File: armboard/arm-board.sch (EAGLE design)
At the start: 50 parts, among them X1 53261-06

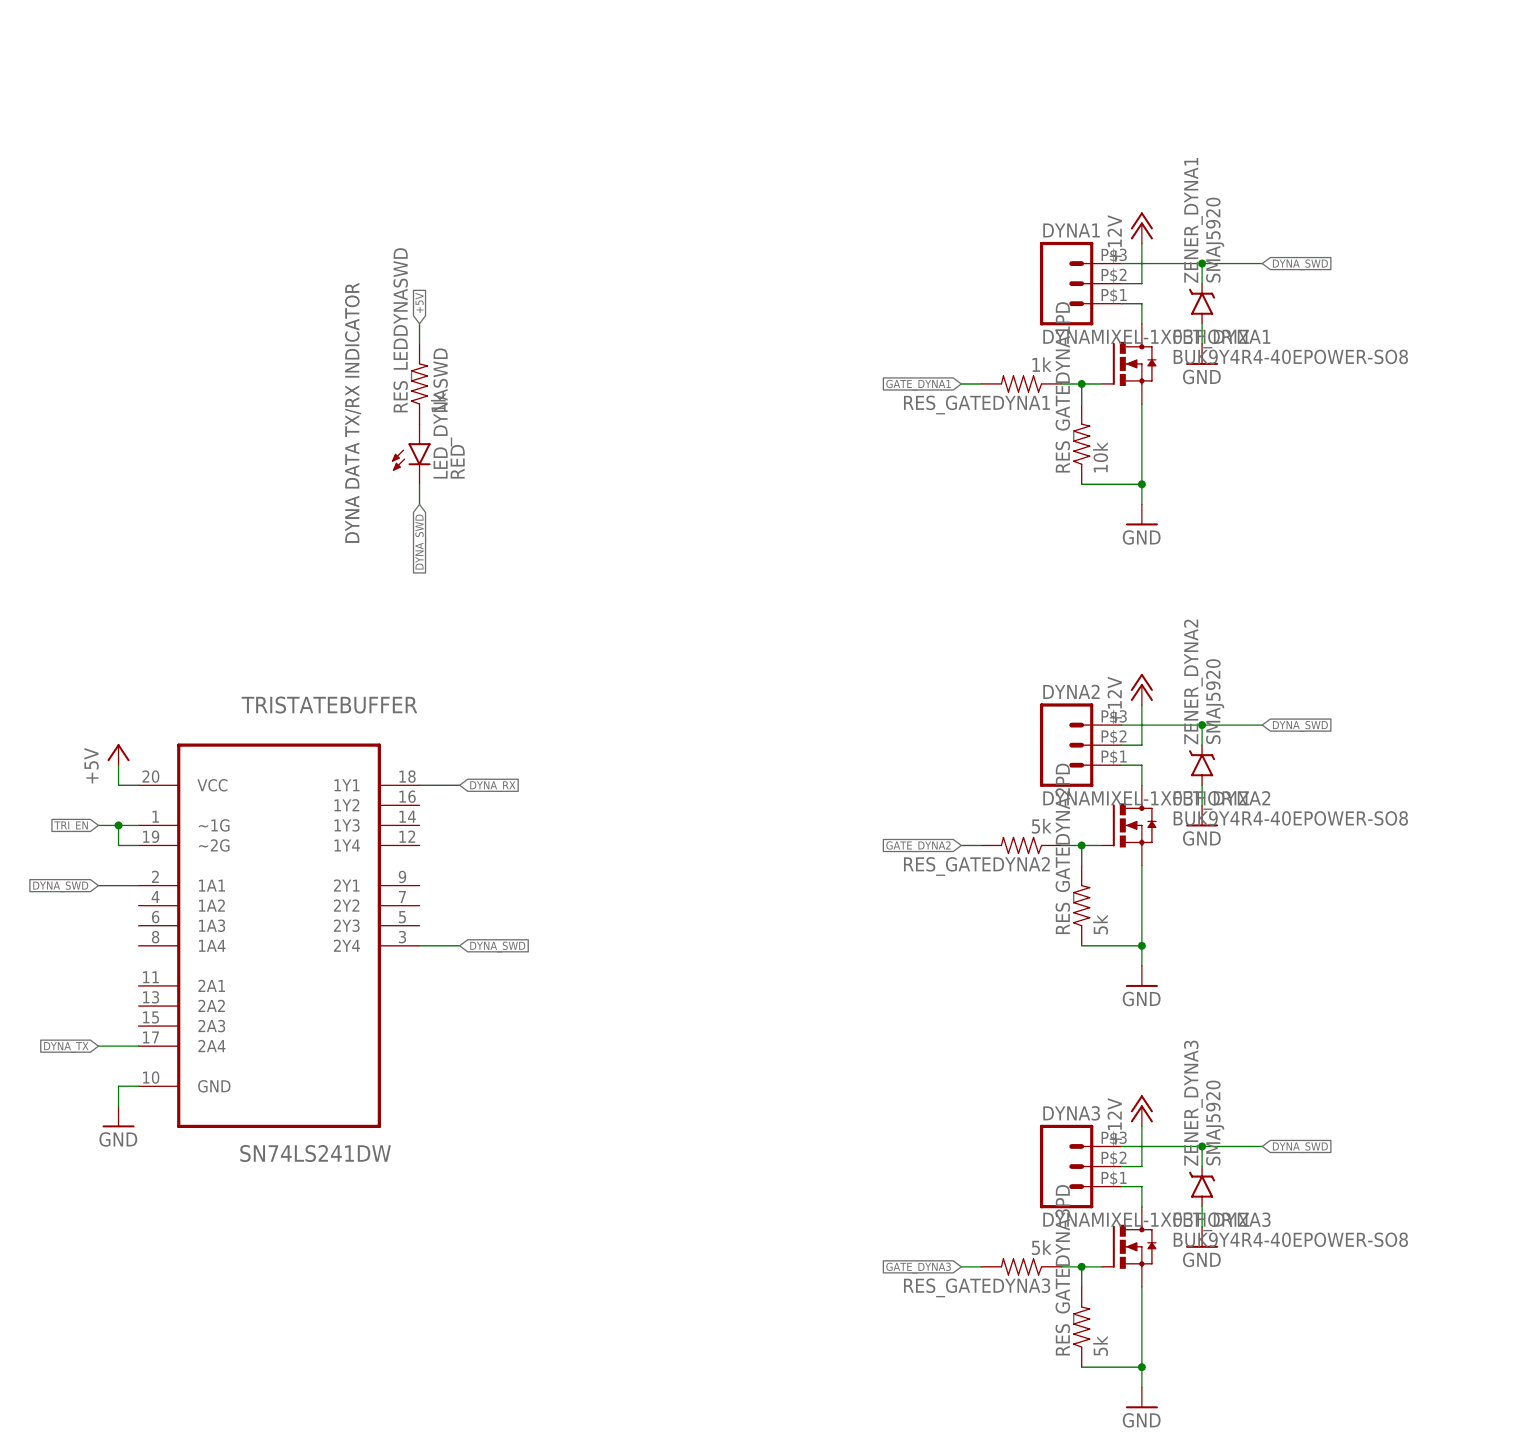
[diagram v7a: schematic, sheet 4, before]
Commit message: added high side fet drivers, rearranged
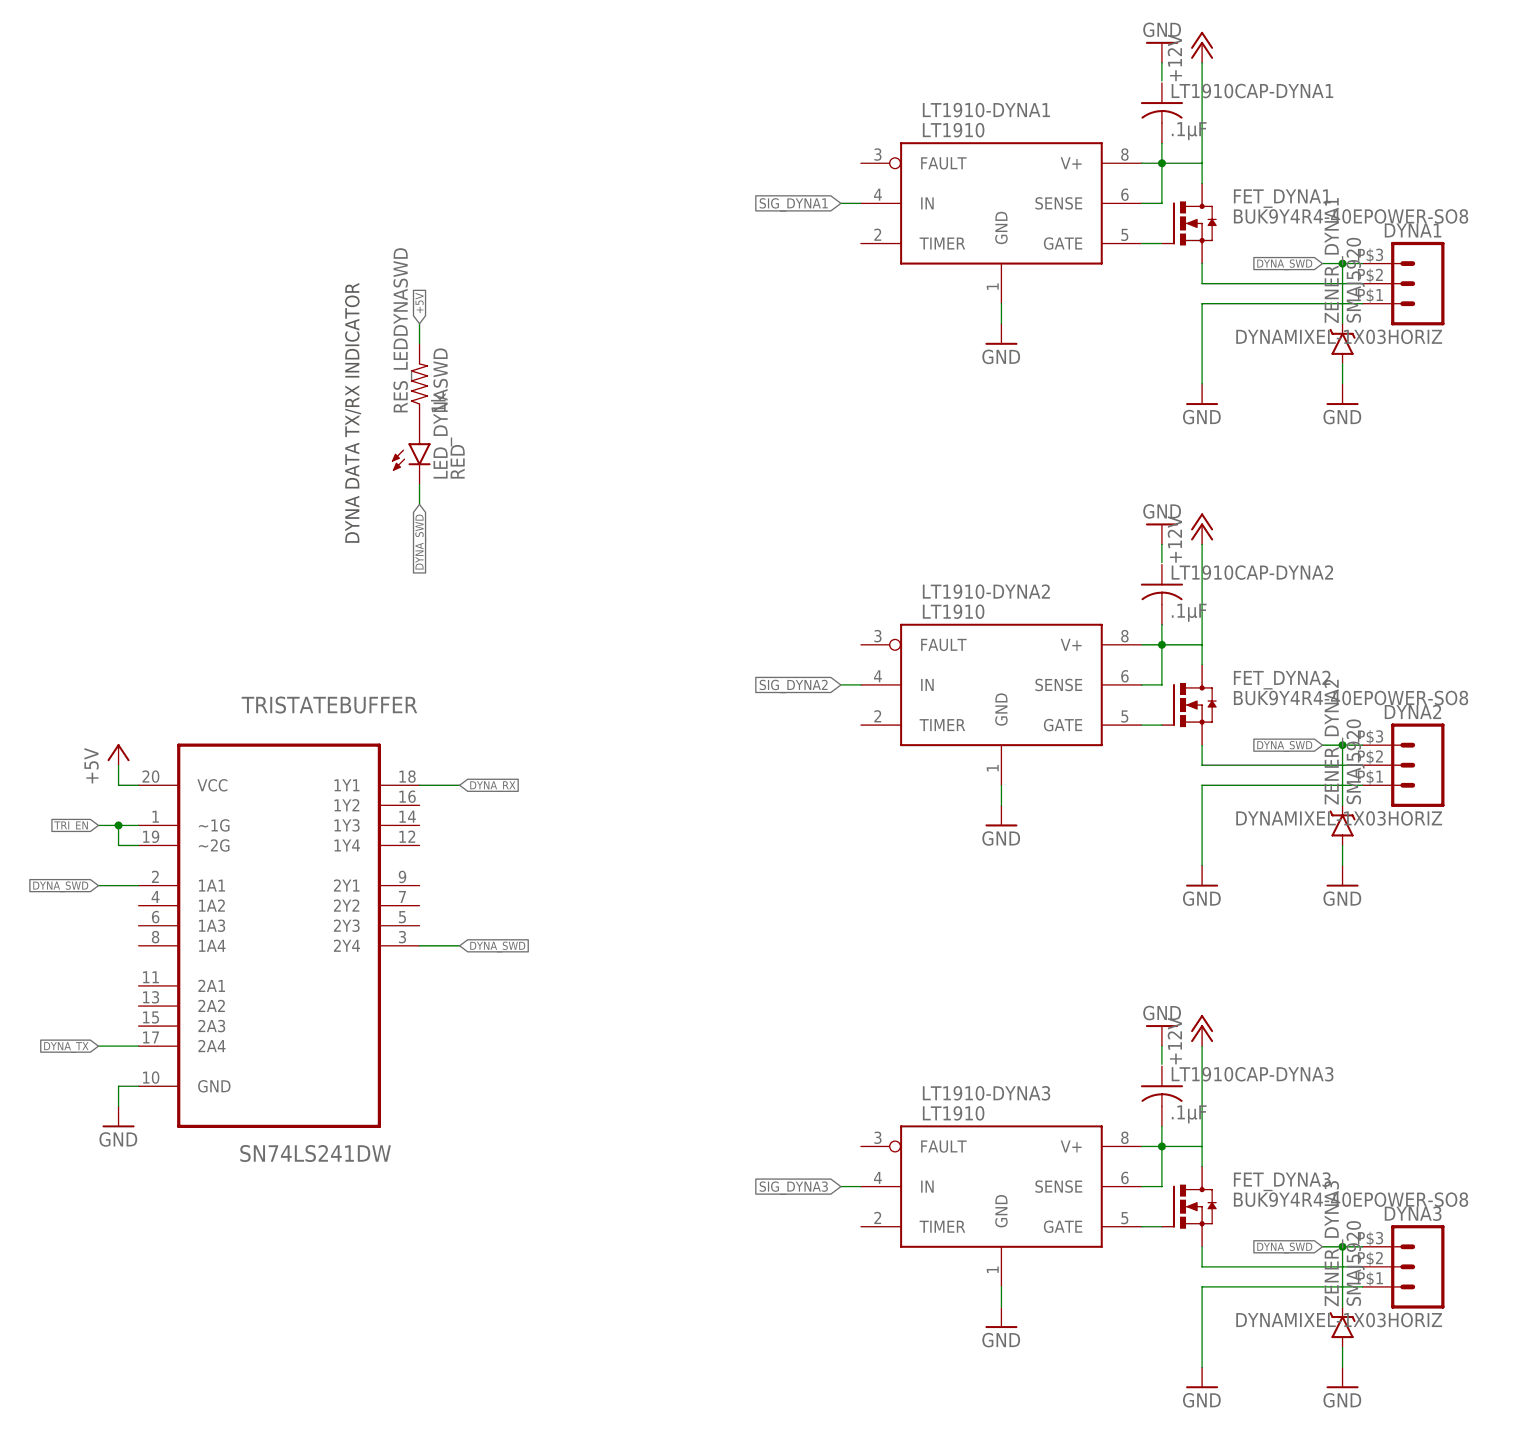
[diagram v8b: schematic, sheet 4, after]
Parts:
- removed C10, C11, C8, C9: 0.33uF, SparkFun-Capacitors:CAP1206
- removed C7: .047uF, SparkFun-Capacitors:CAP1206
- removed CON_PWR_MAIN_J2, CON_PWR_SOL_EE: MLX-2X3-PIN, MRDT-2015-General:MLX-2X3-PIN
- removed MAX232: MAX3232, MRDT-LIB2014:MAX3232
- removed RES_GATEDYNA1: 1k, SparkFun-Resistors:RESISTOR1206
- removed RES_GATEDYNA1PD: 10k, SparkFun-Resistors:RESISTOR1206
- removed RES_GATEDYNA2, RES_GATEDYNA2PD, RES_GATEDYNA3, RES_GATEDYNA3PD, RES_GATEPWREE, RES_GATEPWREEPD, RES_GATEPWRSOL, RES_GATEPWRSOLPD: 5k, SparkFun-Resistors:RESISTOR1206
- added EE-12V, J2_12V, SOL-12V: ANDERSON_POWERPOLEPP45_PCB_HORIZ_RIGHT_2HIGH, MRDT-Connectors:ANDERSON_POWERPOLEPP45_PCB_HORIZ_RIGHT_2HIGH
- added EE-GND, J2_GND, SOL-GND: ANDERSON_POWERPOLEPP45_PCB_HORIZ_RIGHT, MRDT-Connectors:ANDERSON_POWERPOLEPP45_PCB_HORIZ_RIGHT
- added LT1910-DYNA1, LT1910-DYNA2, LT1910-DYNA3, LT1910-EE, LT1910-SOL: LT1910, Jake:LT1910
- added LT1910CAP-DYNA1, LT1910CAP-DYNA2, LT1910CAP-DYNA3, LT1910CAP-EE, LT1910CAP-SOL: .1µF, resistor:C-USC1206
- added MAX232_1: MAX3232SO16, MRDT-Digital-ICs:MAX3232SO16
- added MAX232_C1_1: .047uF, SparkFun-Capacitors:CAP1206
- added MAX232_C2_1, MAX232_VNCAP_1, MAX232_VPCAP_1: 0.33uF, SparkFun-Capacitors:CAP1206
- added MAX232_DECAP_1: 0.1uF, SparkFun-Capacitors:CAP1206
- added PWR_MAIN: APP_3POS_CONFIG5V_12V_VERT, MRDT-Connectors:APP_3POS_CONFIG5V_12V_VERT
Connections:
- removed net DYNA1_GND: DYNA1.1, FET_DYNA1.D
- removed net DYNA1_GND1: DYNA2.1, FET_DYNA2.D
- removed net DYNA1_GND2: DYNA3.1, FET_DYNA3.D
- removed net EE_GND1: CON_PWR_SOL_EE.GND_2, FET_PWREE.D
- removed net GATE_DYNA1: RES_GATEDYNA1.2, U$1.PE2
- removed net GATE_DYNA2: RES_GATEDYNA2.2, U$1.PE3
- removed net GATE_DYNA3: RES_GATEDYNA3.2, U$1.PD7
- removed net GATE_PWR_EE: RES_GATEPWREE.2, U$1.PH0
- removed net GATE_PWR_SOL: RES_GATEPWRSOL.2, U$1.PH1
- removed net N$10: RES_GATEDYNA2.1, RES_GATEDYNA2PD.2
- removed net N$11: FET_PWREE.G, RES_GATEPWREE.1, RES_GATEPWREEPD.2
- removed net N$12: FET_DYNA3.G, RES_GATEDYNA3.1, RES_GATEDYNA3PD.2
- removed net N$15: C7.2, MAX232.C1-
- removed net N$16: C7.1, MAX232.C1+
- removed net N$17: C8.1, MAX232.C2+
- removed net N$18: C8.2, MAX232.C2-
- removed net N$19: C10.1, MAX232.V-
- removed net N$20: C9.1, MAX232.V+
- removed net N$5: CON_PWR_SOL_EE.12V_2
- removed net N$6: FET_DYNA1.G, RES_GATEDYNA1.1, RES_GATEDYNA1PD.2
- removed net N$7: FET_PWRSOL.G, RES_GATEPWRSOL.1, RES_GATEPWRSOLPD.2
- removed net R_OUT1: MAX232.R_OUT1, X1-2.S
- removed net SOL_GND1: CON_PWR_SOL_EE.GND_1, FET_PWRSOL.D
- removed net T_OUT1: MAX232.T_OUT1, X1-1.S
- removed net VCC1: C11.1, MAX232.VCC
- new net GATE-DYNA1: LT1910-DYNA1.GATE
- new net GATE-DYNA2: LT1910-DYNA2.GATE
- new net GATE-DYNA3: LT1910-DYNA3.GATE
- new net GATE-EE: LT1910-EE.GATE
- new net GATE-SOL: LT1910-SOL.GATE
- new net N$1_1: MAX232_1.C1+, MAX232_C1_1.1
- new net N$2_1: MAX232_1.V+, MAX232_VPCAP_1.1
- new net N$3_1: MAX232_1.C1-, MAX232_C1_1.2
- new net N$4_1: MAX232_1.C2+, MAX232_C2_1.1
- new net N$5_1: MAX232_1.C2-, MAX232_C2_1.2
- new net N$6_1: MAX232_1.V-, MAX232_VNCAP_1.1
- new net R1IN: MAX232_1.R1IN, X1-2.S
- new net SIG_DYNA1: LT1910-DYNA1.IN, U$1.PE2
- new net SIG_DYNA2: LT1910-DYNA2.IN, U$1.PE3
- new net SIG_DYNA3: LT1910-DYNA3.IN, U$1.PD7
- new net SIG_EE: LT1910-EE.IN, U$1.PH0
- new net SIG_SOL: LT1910-SOL.IN, U$1.PH1
- new net SOURCE-DYNA1: DYNA1.2, FET_DYNA1.S
- new net SOURCE-DYNA2: DYNA2.2, FET_DYNA2.S
- new net SOURCE-DYNA3: DYNA3.2, FET_DYNA3.S
- new net SOURCE-EE: EE-12V.P$1, FET_PWREE.S
- new net SOURCE-SOL: FET_PWRSOL.S, SOL-12V.P$1
- new net T1OUT: MAX232_1.T1OUT, X1-1.S
- net +12V: now also FET_DYNA1.D, FET_DYNA2.D, FET_DYNA3.D, FET_PWREE.D, FET_PWRSOL.D, J2_12V.P$1, LT1910-DYNA1.SENSE, LT1910-DYNA1.V+, LT1910-DYNA2.SENSE, LT1910-DYNA2.V+, LT1910-DYNA3.SENSE, LT1910-DYNA3.V+, LT1910-EE.SENSE, LT1910-EE.V+, LT1910-SOL.SENSE, LT1910-SOL.V+, LT1910CAP-DYNA1.2, LT1910CAP-DYNA2.2, LT1910CAP-DYNA3.2, LT1910CAP-EE.2, LT1910CAP-SOL.2, PWR_MAIN12V.P$1, RES_LEDPWR.2; no longer CON_PWR_MAIN_J2.12V_1, CON_PWR_MAIN_J2.12V_2, CON_PWR_SOL_EE.12V_1, DYNA1.2, DYNA2.2, DYNA3.2
- net +5V: now also MAX232_1.VCC, MAX232_DECAP_1.2, PWR_MAIN5V.P$1; no longer CON_PWR_MAIN_J2.5V_1, RES_LEDPWR.2
- net DYNA_RX: now also U$1.PC4; no longer U$1.PC6
- net DYNA_TX: now also U$1.PC5; no longer U$1.PC7
- net GND: now also DYNA1.1, DYNA2.1, DYNA3.1, EE-GND.P$1, J2_GND.P$1, LT1910-DYNA1.GND, LT1910-DYNA2.GND, LT1910-DYNA3.GND, LT1910-EE.GND, LT1910-SOL.GND, LT1910CAP-EE.1, LT1910CAP-SOL.1, MAX232_1.GND, MAX232_DECAP_1.1, MAX232_VNCAP_1.2, MAX232_VPCAP_1.2, PWR_MAINGND.P$1, SOL-GND.P$1; no longer C10.2, C11.2, C9.2, CON_PWR_MAIN_J2.GND_1, CON_PWR_MAIN_J2.GND_2, FET_DYNA1.S, FET_DYNA2.S, FET_DYNA3.S, FET_PWREE.S, FET_PWRSOL.S, MAX232.GND, RES_GATEDYNA1PD.1, RES_GATEDYNA2PD.1, RES_GATEDYNA3PD.1, RES_GATEPWREEPD.1, RES_GATEPWRSOLPD.1
- net J2_RS232RX: now also MAX232_1.R1OUT; no longer MAX232.R_IN1
- net J2_RS232TX: now also MAX232_1.T1IN; no longer MAX232.T_IN1
- net XB_RX: now also U$1.PC6; no longer U$1.PQ3/PA2
- net XB_TX: now also U$1.PC7; no longer U$1.PQ2/PA3
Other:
- note added: "END EFFECTOR POWER"
- note added: "J2 POWER"
- note added: "MAIN POWER"
- note added: "SOLENOID POWER"
- note removed: "PWR_EE"
- note removed: "PWR_J2"
- note removed: "PWR_MAIN"
- note removed: "PWR_SOL"
- moved on the sheet: DYNA1, DYNA2, DYNA3, FET_DYNA1, FET_DYNA2, FET_DYNA3, FET_PWREE, FET_PWRSOL, X1-1, X1-2, X1-3, X1-4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
